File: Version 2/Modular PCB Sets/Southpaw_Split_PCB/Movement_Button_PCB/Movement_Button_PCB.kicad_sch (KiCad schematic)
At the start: 12 parts

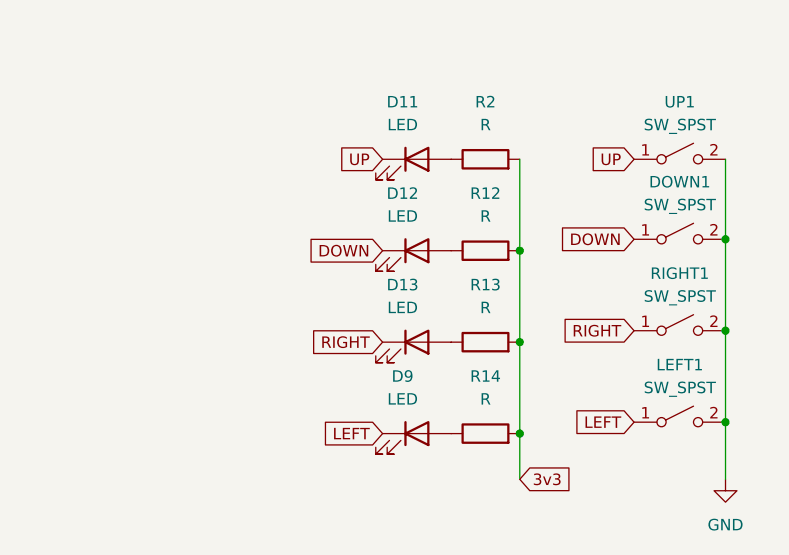
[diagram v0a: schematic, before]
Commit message: rework for schematic structure to accomodate new pico symbol and jst connectors
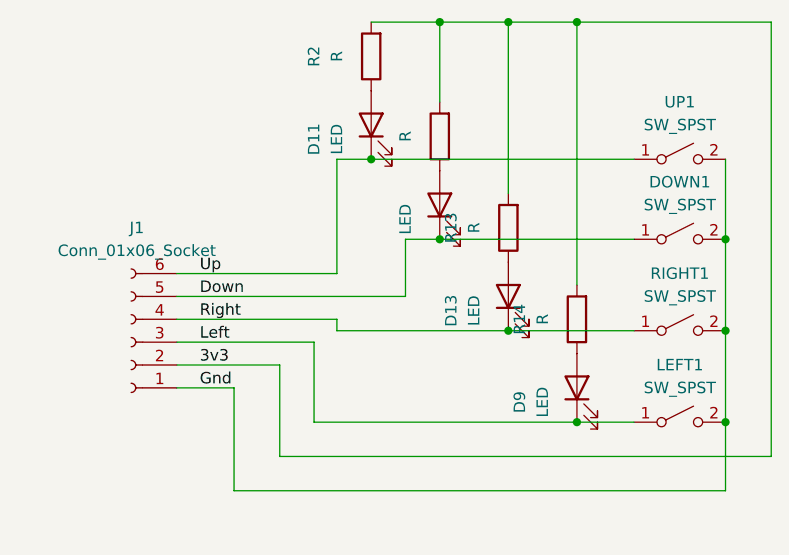
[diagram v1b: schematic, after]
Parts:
- added J1: Conn_01x06_Socket, Connector_JST:JST_PH_B6B-PH-K_1x06_P2.00mm_Vertical, symbol Connector:Conn_01x06_Socket
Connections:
- net 3v3: now also J1.2 (Pin_2)
- net DOWN renamed Down
- net Down: now also J1.5 (Pin_5)
- net GND renamed Gnd
- net Gnd: now also J1.1 (Pin_1)
- net LEFT renamed Left
- net Left: now also J1.3 (Pin_3)
- net RIGHT renamed Right
- net Right: now also J1.4 (Pin_4)
- net UP renamed Up
- net Up: now also J1.6 (Pin_6)
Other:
- moved on the sheet: D11, D13, D9, R13, R14, R2

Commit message: created footprints for all lockout and oled display
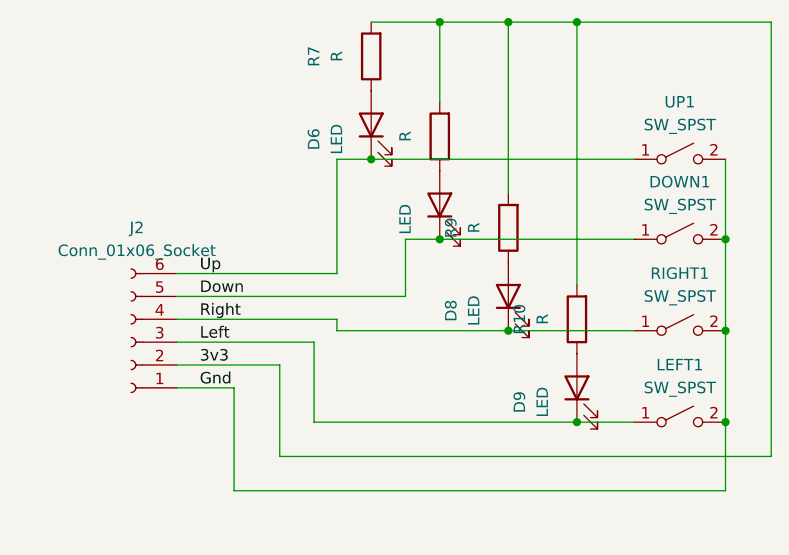
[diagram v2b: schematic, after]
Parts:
- renumbered D11 to D6, D12 to D7, D13 to D8, J1 to J2, R14 to R10, R2 to R7, R12 to R8, R13 to R9
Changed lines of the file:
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@@
 		)
 		(instances
+			(project "Southpaw_Split_PCB"
+				(path "/12c03e98-16e3-4861-a1ce-d2b4d8ad36ee/c50547d5-3763-4872-bd17-a45caaa5aee4"
+					(reference "UP1")
+					(unit 1)
+				)
+			)
 			(project "Movement_Button_PCB"
 				(path "/2a11653f-1472-4e75-80b8-426c064cfc86"
@@
 		(dnp no)
 		(fields_autoplaced yes)
-		(property "Reference" "D12"
+		(property "Reference" "D7"
 			(at 115.57 85.4075 0)
 			(effects
@@
 		)
 		(instances
+			(project "Southpaw_Split_PCB"
+				(path "/12c03e98-16e3-4861-a1ce-d2b4d8ad36ee/c50547d5-3763-4872-bd17-a45caaa5aee4"
+					(reference "D7")
+					(unit 1)
+				)
+			)
 			(project "Movement_Button_PCB"
 				(path "/2a11653f-1472-4e75-80b8-426c064cfc86"
@@
 		(dnp no)
 		(fields_autoplaced yes)
-		(property "Reference" "D13"
+		(property "Reference" "D8"
 			(at 123.19 95.5675 0)
 			(effects
@@
 		)
 		(instances
+			(project "Southpaw_Split_PCB"
+				(path "/12c03e98-16e3-4861-a1ce-d2b4d8ad36ee/c50547d5-3763-4872-bd17-a45caaa5aee4"
+					(reference "D8")
+					(unit 1)
+				)
+			)
 			(project "Movement_Button_PCB"
 				(path "/2a11653f-1472-4e75-80b8-426c064cfc86"
@@
 		(dnp no)
 		(fields_autoplaced yes)
-		(property "Reference" "R12"
+		(property "Reference" "R8"
 			(at 115.57 76.2 90)
 			(effects
@@
 		)
 		(instances
+			(project "Southpaw_Split_PCB"
+				(path "/12c03e98-16e3-4861-a1ce-d2b4d8ad36ee/c50547d5-3763-4872-bd17-a45caaa5aee4"
+					(reference "R8")
+					(unit 1)
+				)
+			)
 			(project "Movement_Button_PCB"
 				(path "/2a11653f-1472-4e75-80b8-426c064cfc86"
@@
 		)
 		(instances
+			(project "Southpaw_Split_PCB"
+				(path "/12c03e98-16e3-4861-a1ce-d2b4d8ad36ee/c50547d5-3763-4872-bd17-a45caaa5aee4"
+					(reference "RIGHT1")
+					(unit 1)
+				)
+			)
 			(project "Movement_Button_PCB"
 				(path "/2a11653f-1472-4e75-80b8-426c064cfc86"
@@
 		(dnp no)
 		(fields_autoplaced yes)
-		(property "Reference" "J1"
+		(property "Reference" "J2"
 			(at 88.265 86.36 0)
 			(effects
@@
 		)
 		(instances
+			(project "Southpaw_Split_PCB"
+				(path "/12c03e98-16e3-4861-a1ce-d2b4d8ad36ee/c50547d5-3763-4872-bd17-a45caaa5aee4"
+					(reference "J2")
+					(unit 1)
+				)
+			)
 			(project ""
 				(path "/2a11653f-1472-4e75-80b8-426c064cfc86"
@@
 		(dnp no)
 		(fields_autoplaced yes)
-		(property "Reference" "R2"
+		(property "Reference" "R7"
 			(at 107.95 67.31 90)
 			(effects
@@
 		)
 		(instances
+			(project "Southpaw_Split_PCB"
+				(path "/12c03e98-16e3-4861-a1ce-d2b4d8ad36ee/c50547d5-3763-4872-bd17-a45caaa5aee4"
+					(reference "R7")
+					(unit 1)
+				)
+			)
 			(project "Movement_Button_PCB"
 				(path "/2a11653f-1472-4e75-80b8-426c064cfc86"
@@
 		(dnp no)
 		(fields_autoplaced yes)
-		(property "Reference" "R13"
+		(property "Reference" "R9"
 			(at 123.19 86.36 90)
 			(effects
@@
 		)
 		(instances
+			(project "Southpaw_Split_PCB"
+				(path "/12c03e98-16e3-4861-a1ce-d2b4d8ad36ee/c50547d5-3763-4872-bd17-a45caaa5aee4"
+					(reference "R9")
+					(unit 1)
+				)
+			)
 			(project "Movement_Button_PCB"
 				(path "/2a11653f-1472-4e75-80b8-426c064cfc86"
@@
 		)
 		(instances
+			(project "Southpaw_Split_PCB"
+				(path "/12c03e98-16e3-4861-a1ce-d2b4d8ad36ee/c50547d5-3763-4872-bd17-a45caaa5aee4"
+					(reference "LEFT1")
+					(unit 1)
+				)
+			)
 			(project "Movement_Button_PCB"
 				(path "/2a11653f-1472-4e75-80b8-426c064cfc86"
@@
 		(on_board yes)
 		(dnp no)
-		(property "Reference" "D11"
+		(property "Reference" "D6"
 			(at 107.95 76.5175 0)
 			(effects
@@
 		)
 		(instances
+			(project "Southpaw_Split_PCB"
+				(path "/12c03e98-16e3-4861-a1ce-d2b4d8ad36ee/c50547d5-3763-4872-bd17-a45caaa5aee4"
+					(reference "D6")
+					(unit 1)
+				)
+			)
 			(project "Movement_Button_PCB"
 				(path "/2a11653f-1472-4e75-80b8-426c064cfc86"
@@
 		)
 		(instances
+			(project "Southpaw_Split_PCB"
+				(path "/12c03e98-16e3-4861-a1ce-d2b4d8ad36ee/c50547d5-3763-4872-bd17-a45caaa5aee4"
+					(reference "D9")
+					(unit 1)
+				)
+			)
 			(project "Movement_Button_PCB"
 				(path "/2a11653f-1472-4e75-80b8-426c064cfc86"
@@
 		)
 		(instances
+			(project "Southpaw_Split_PCB"
+				(path "/12c03e98-16e3-4861-a1ce-d2b4d8ad36ee/c50547d5-3763-4872-bd17-a45caaa5aee4"
+					(reference "DOWN1")
+					(unit 1)
+				)
+			)
 			(project "Movement_Button_PCB"
 				(path "/2a11653f-1472-4e75-80b8-426c064cfc86"
@@
 		(dnp no)
 		(fields_autoplaced yes)
-		(property "Reference" "R14"
+		(property "Reference" "R10"
 			(at 130.81 96.52 90)
 			(effects
@@
 		)
 		(instances
-			(project "Movement_Button_PCB"
-				(path "/2a11653f-1472-4e75-80b8-426c064cfc86"
+			(project "Southpaw_Split_PCB"
+				(path "/12c03e98-16e3-4861-a1ce-d2b4d8ad36ee/c50547d5-3763-4872-bd17-a45caaa5aee4"
+					(reference "R10")
+					(unit 1)
+				)
+			)
+			(project "Movement_Button_PCB"
+				(path "/2a11653f-1472-4e75-80b8-426c064cfc86"

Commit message: general part layout
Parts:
- renumbered DOWN1 to DOWN6, J2 to J6, LEFT1 to LEFT6, R7 to R6, R8 to R7, R9 to R8, R10 to R9, RIGHT1 to RIGHT6, UP1 to UP6
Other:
- moved on the sheet: D6, D8, D9, DOWN6, J6, LEFT6, R6, R8, R9, RIGHT6, UP6

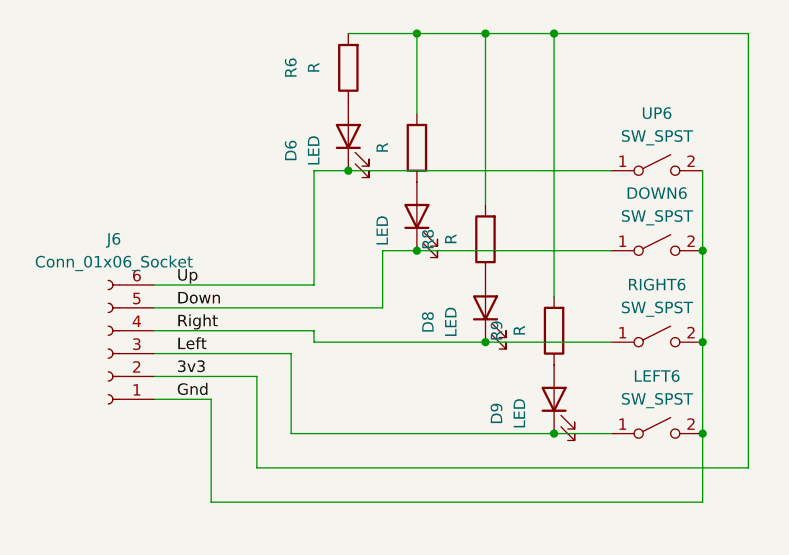
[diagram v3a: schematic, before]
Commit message: finished movement pcb, need to make some small adjustments to action pcb
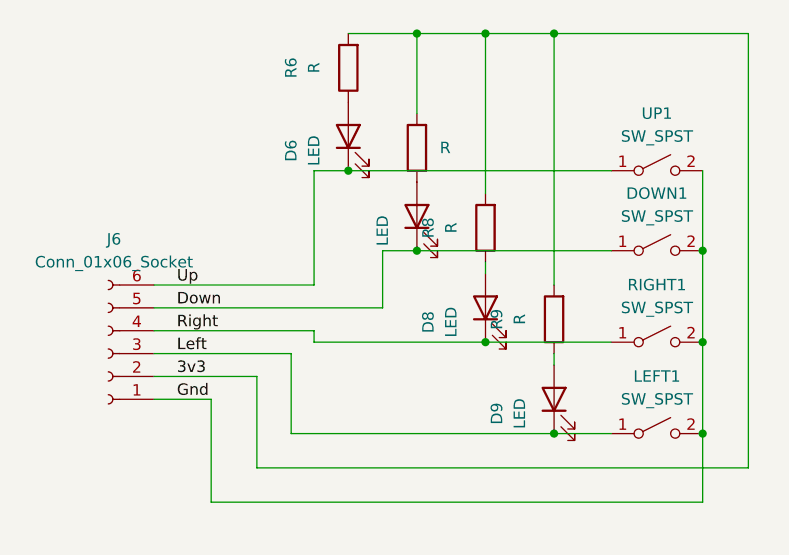
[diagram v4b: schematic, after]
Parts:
- renumbered DOWN6 to DOWN1, LEFT6 to LEFT1, RIGHT6 to RIGHT1, UP6 to UP1
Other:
- moved on the sheet: R8, R9
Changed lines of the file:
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@@
 	(wire
 		(pts
-			(xy 134.62 93.98) (xy 134.62 64.77)
+			(xy 134.62 92.71) (xy 134.62 64.77)
 		)
 		(stroke
@@
 	(wire
 		(pts
+			(xy 134.62 100.33) (xy 134.62 101.6)
+		)
+		(stroke
+			(width 0)
+			(type default)
+		)
+	)
+	(wire
+		(pts
+			(xy 127 90.17) (xy 127 91.44)
+		)
+		(stroke
+			(width 0)
+			(type default)
+		)
+	)
+	(wire
+		(pts
 			(xy 115.57 88.9) (xy 119.38 88.9)
 		)
@@
 	(wire
 		(pts
-			(xy 127 64.77) (xy 127 83.82)
+			(xy 127 64.77) (xy 127 82.55)
 		)
 		(stroke
@@
 		(dnp no)
 		(fields_autoplaced yes)
-		(property "Reference" "UP6"
+		(property "Reference" "UP1"
 			(at 146.05 73.66 0)
 			(effects
@@
 			(project "Movement_Button_PCB"
 				(path "/2a11653f-1472-4e75-80b8-426c064cfc86"
-					(reference "UP6")
+					(reference "UP1")
 					(unit 1)
 				)
@@
 		)
 		(property "Value" "R"
-			(at 115.57 77.47 90)
-			(effects
-				(font
-					(size 1.27 1.27)
-				)
+			(at 121.92 77.4699 0)
+			(effects
+				(font
+					(size 1.27 1.27)
+				)
+				(justify right)
 			)
 		)
@@
 		(dnp no)
 		(fields_autoplaced yes)
-		(property "Reference" "RIGHT6"
+		(property "Reference" "RIGHT1"
 			(at 146.05 92.71 0)
 			(effects
@@
 			(project "Movement_Button_PCB"
 				(path "/2a11653f-1472-4e75-80b8-426c064cfc86"
-					(reference "RIGHT6")
+					(reference "RIGHT1")
 					(unit 1)
 				)
@@
 	(symbol
 		(lib_id "Device:R")
-		(at 127 87.63 180)
+		(at 127 86.36 180)
 		(unit 1)
 		(exclude_from_sim no)
@@
 		(fields_autoplaced yes)
 		(property "Reference" "R8"
-			(at 120.65 87.63 90)
+			(at 120.65 86.36 90)
 			(effects
 				(font
@@
 		)
 		(property "Value" "R"
-			(at 123.19 87.63 90)
+			(at 123.19 86.36 90)
 			(effects
 				(font
@@
 		)
 		(property "Footprint" "Resistor_THT:R_Axial_DIN0207_L6.3mm_D2.5mm_P10.16mm_Horizontal"
-			(at 128.778 87.63 90)
+			(at 128.778 86.36 90)
 			(effects
 				(font
@@
 		)
 		(property "Datasheet" "~"
-			(at 127 87.63 0)
+			(at 127 86.36 0)
 			(effects
 				(font
@@
 		)
 		(property "Description" "Resistor"
-			(at 127 87.63 0)
+			(at 127 86.36 0)
 			(effects
 				(font
@@
 		(dnp no)
 		(fields_autoplaced yes)
-		(property "Reference" "LEFT6"
+		(property "Reference" "LEFT1"
 			(at 146.05 102.87 0)
 			(effects
@@
 			(project "Movement_Button_PCB"
 				(path "/2a11653f-1472-4e75-80b8-426c064cfc86"
-					(reference "LEFT6")
+					(reference "LEFT1")
 					(unit 1)
 				)
@@
 		(dnp no)
 		(fields_autoplaced yes)
-		(property "Reference" "DOWN6"
+		(property "Reference" "DOWN1"
 			(at 146.05 82.55 0)
 			(effects
@@
 			(project "Movement_Button_PCB"
 				(path "/2a11653f-1472-4e75-80b8-426c064cfc86"
-					(reference "DOWN6")
+					(reference "DOWN1")
 					(unit 1)
 				)
@@
 	(symbol
 		(lib_id "Device:R")
-		(at 134.62 97.79 180)
+		(at 134.62 96.52 180)
 		(unit 1)
 		(exclude_from_sim no)
@@
 		(fields_autoplaced yes)
 		(property "Reference" "R9"
-			(at 128.27 97.79 90)
+			(at 128.27 96.52 90)
 			(effects
 				(font
@@
 		)
 		(property "Value" "R"
-			(at 130.81 97.79 90)
+			(at 130.81 96.52 90)
 			(effects
 				(font
@@
 		)
 		(property "Footprint" "Resistor_THT:R_Axial_DIN0207_L6.3mm_D2.5mm_P10.16mm_Horizontal"
-			(at 136.398 97.79 90)
+			(at 136.398 96.52 90)
 			(effects
 				(font
@@
 		)
 		(property "Datasheet" "~"
-			(at 134.62 97.79 0)
+			(at 134.62 96.52 0)
 			(effects
 				(font
@@
 		)
 		(property "Description" "Resistor"
-			(at 134.62 97.79 0)
-			(effects
-				(font
+			(at 134.62 96.52 0)
+			(effects
+				(font
